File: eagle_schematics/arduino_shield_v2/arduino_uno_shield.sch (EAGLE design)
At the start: 20 parts

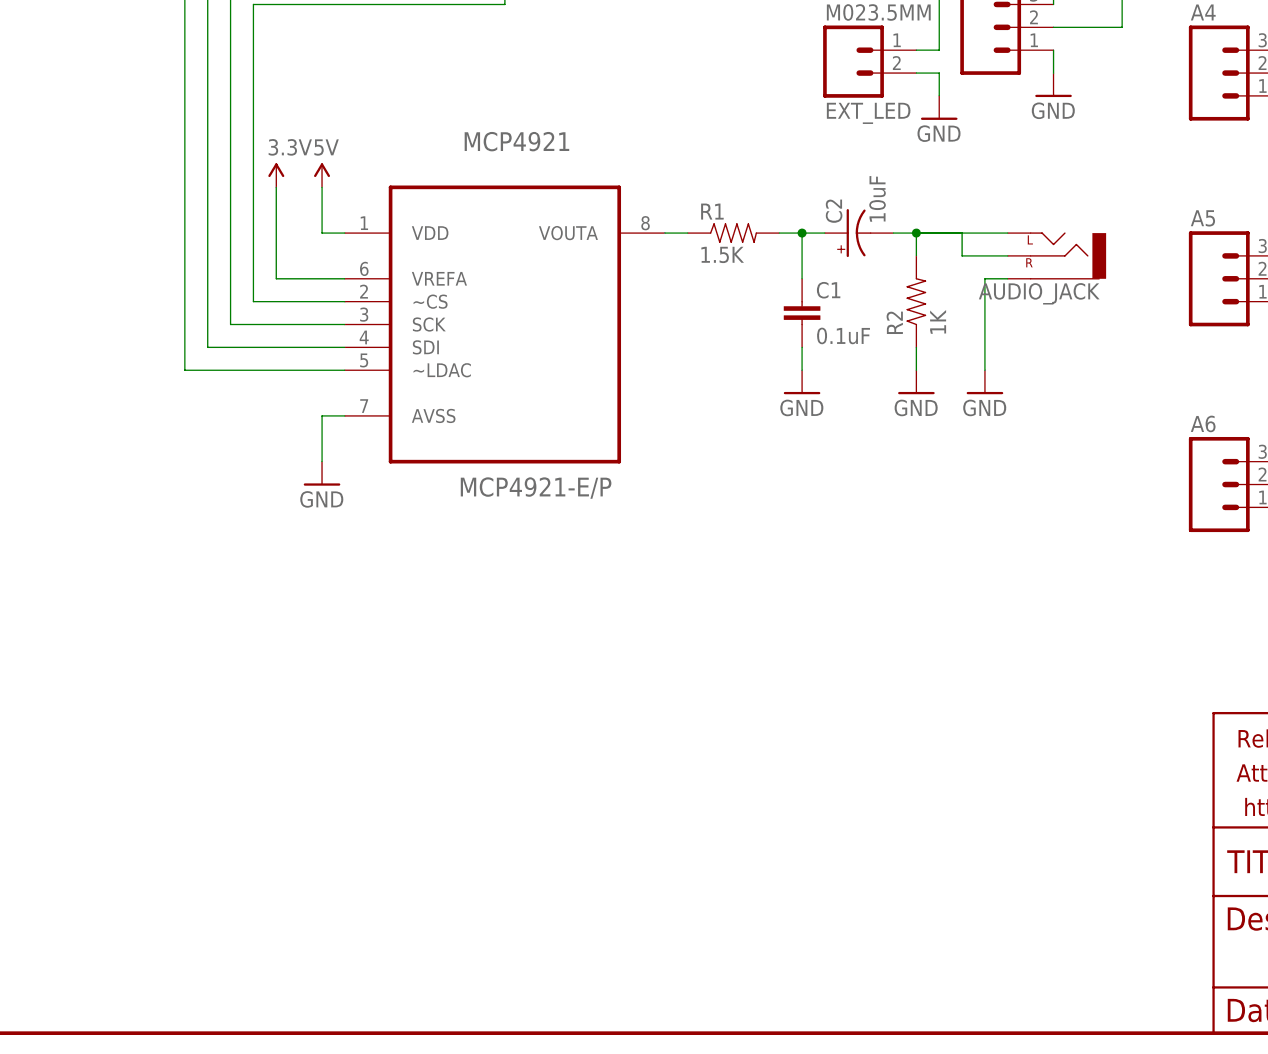
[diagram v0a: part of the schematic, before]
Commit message: add amplifier
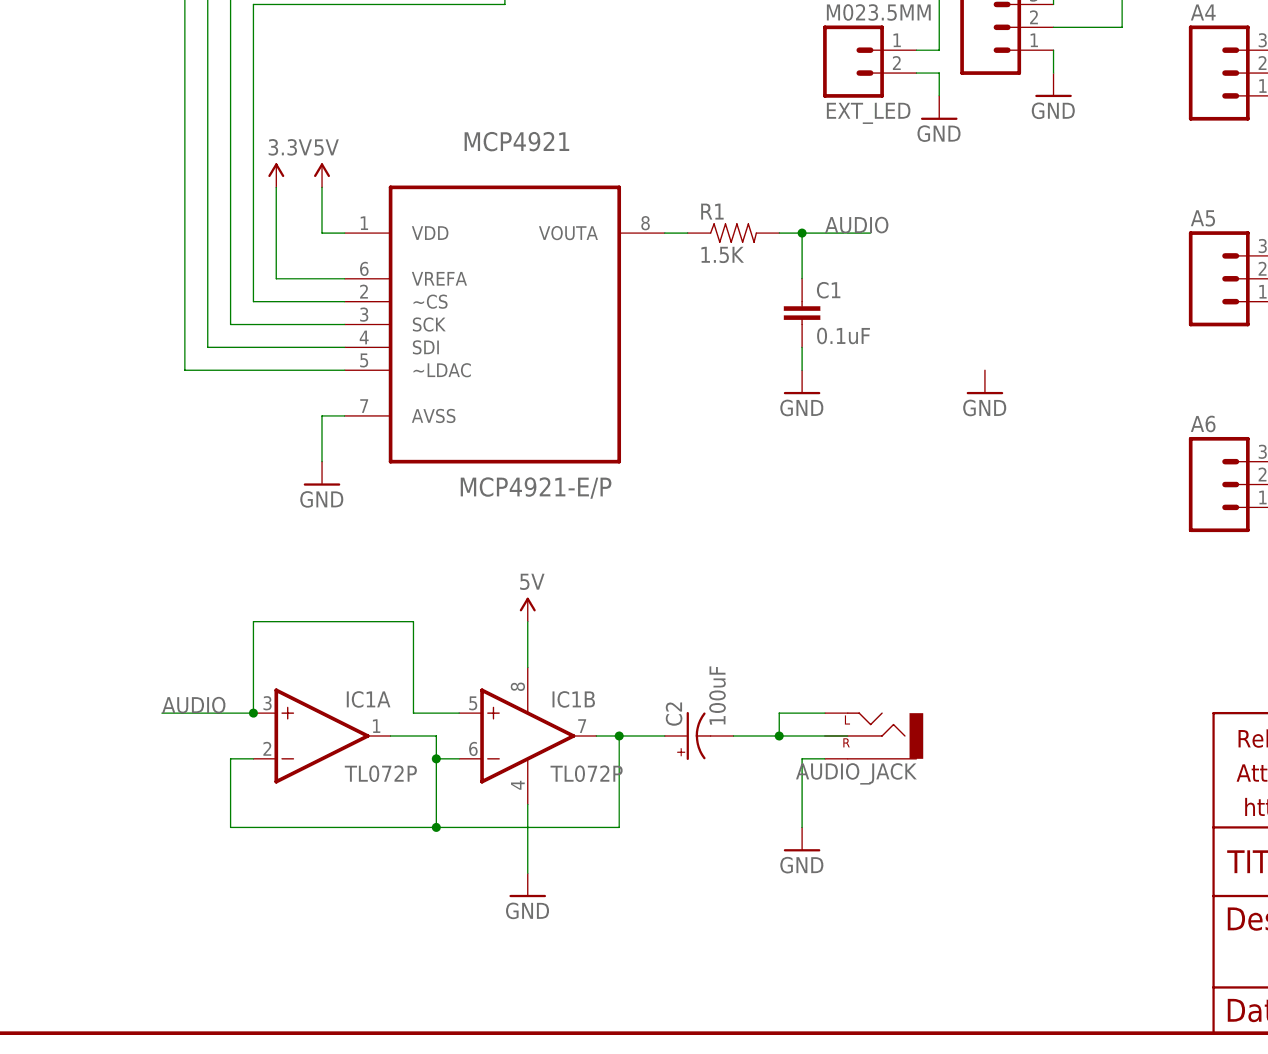
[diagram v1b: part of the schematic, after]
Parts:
- removed R2: 1K, SparkFun-Passives:RESISTORPTH-1/4W
- added IC1: TL072P, linear:TL072P
- C2: value 10uF -> 100uF; device SparkFun-Passives:CAP_POLPTH2 -> SparkFun-Capacitors:CAP_POLPTH1
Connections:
- removed net N$8: C1.1, C2.+, R1.2
- removed net N$9: AUDIO_JACK.LEFT, AUDIO_JACK.RIGHT, C2.-, R2.2
- new net AUDIO: C1.1, IC1A.+IN, IC1B.+IN, R1.2
- new net N$4: C2.+, IC1A.-IN, IC1A.OUT, IC1B.-IN, IC1B.OUT
- new net N$5: AUDIO_JACK.LEFT, C2.-
- net 5V: now also IC1P.V+
- net GND: now also IC1P.V-; no longer R2.1
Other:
- moved on the sheet: AUDIO_JACK, C2
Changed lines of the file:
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@@
 <?xml version="1.0" encoding="utf-8"?>
 <!DOCTYPE eagle SYSTEM "eagle.dtd">
-<eagle version="7.1.0">
+<eagle version="7.5.0">
 <drawing>
 <settings>
@@
 <layer number="223" name="223bmp" color="24" fill="1" visible="no" active="no"/>
 <layer number="224" name="224bmp" color="25" fill="1" visible="no" active="no"/>
+<layer number="225" name="225bmp" color="7" fill="1" visible="yes" active="yes"/>
+<layer number="226" name="226bmp" color="7" fill="1" visible="yes" active="yes"/>
+<layer number="227" name="227bmp" color="7" fill="1" visible="yes" active="yes"/>
+<layer number="228" name="228bmp" color="7" fill="1" visible="yes" active="yes"/>
+<layer number="229" name="229bmp" color="7" fill="1" visible="yes" active="yes"/>
+<layer number="230" name="230bmp" color="7" fill="1" visible="yes" active="yes"/>
+<layer number="231" name="231bmp" color="7" fill="1" visible="yes" active="yes"/>
 <layer number="248" name="Housing" color="7" fill="1" visible="yes" active="yes"/>
 <layer number="249" name="Edge" color="7" fill="1" visible="yes" active="yes"/>
@@
 <layer number="251" name="SMDround" color="12" fill="11" visible="no" active="no"/>
 <layer number="254" name="cooling" color="7" fill="1" visible="yes" active="yes"/>
+<layer number="255" name="routoute" color="7" fill="1" visible="yes" active="yes"/>
 </layers>
 <schematic xreflabel="%F%N/%S.%C%R" xrefpart="/%S.%C%R">
@@
 <part name="MCP4921" library="Microchip_By_element14_Batch_1" deviceset="MCP4921-E/P" device=""/>
 <part name="GND1" library="SparkFun-Aesthetics" deviceset="GND" device=""/>
-<part name="R2" library="SparkFun-Passives" deviceset="RESISTOR" device="PTH-1/4W" value="1K"/>
 <part name="AUDIO_JACK" library="SparkFun-Connectors" deviceset="AUDIO-JACK" device="PTH"/>
 <part name="A1" library="SparkFun-Connectors" deviceset="M03" device="PTH"/>
@@
 <part name="R1" library="SparkFun-Passives" deviceset="RESISTOR" device="PTH-1/4W" value="1.5K"/>
 <part name="C1" library="SparkFun-Passives" deviceset="CAP" device="PTH" value="0.1uF"/>
-<part name="C2" library="SparkFun-Passives" deviceset="CAP_POL" device="PTH2" value="10uF"/>
 <part name="GND6" library="SparkFun-Aesthetics" deviceset="GND" device=""/>
 <part name="GND7" library="SparkFun-Aesthetics" deviceset="GND" device=""/>
@@
 <part name="EXT_LED" library="SparkFun-Connectors" deviceset="M02" device="3.5MM"/>
 <part name="FRAME3" library="SparkFun-Aesthetics" deviceset="FRAME-LETTER" device=""/>
+<part name="IC1" library="linear" deviceset="TL072" device="P"/>
+<part name="SUPPLY15" library="SparkFun-Aesthetics" deviceset="5V" device=""/>
+<part name="C2" library="SparkFun-Capacitors" deviceset="CAP_POL" device="PTH1" value="100uF"/>
+<part name="GND15" library="SparkFun-Aesthetics" deviceset="GND" device=""/>
 </parts>
 <sheets>
@@
 <instance part="MCP4921" gate="A" x="-101.6" y="2.54"/>
 <instance part="GND1" gate="1" x="-68.58" y="-7.62"/>
-<instance part="R2" gate="G$1" x="-55.88" y="2.54" rot="R90"/>
-<instance part="AUDIO_JACK" gate="G$1" x="-40.64" y="7.62" rot="R180"/>
+<instance part="AUDIO_JACK" gate="G$1" x="-60.96" y="-45.72" rot="R180"/>
 <instance part="A1" gate="G$1" x="-48.26" y="55.88" smashed="yes">
 <attribute name="VALUE" x="-50.8" y="48.26" size="1.778" layer="96"/>
@@
 <instance part="R1" gate="G$1" x="-76.2" y="10.16"/>
 <instance part="C1" gate="G$1" x="-68.58" y="0"/>
-<instance part="C2" gate="G$1" x="-63.5" y="10.16" rot="R90"/>
-<instance part="GND6" gate="1" x="-55.88" y="-7.62"/>
+<instance part="GND6" gate="1" x="-99.06" y="-63.5"/>
 <instance part="GND7" gate="1" x="-48.26" y="-7.62"/>
 <instance part="GND8" gate="1" x="-121.92" y="-17.78"/>
@@
 <instance part="FRAME3" gate="G$1" x="-170.18" y="-78.74"/>
 <instance part="FRAME3" gate="G$2" x="-22.86" y="-78.74"/>
+<instance part="IC1" gate="A" x="-121.92" y="-45.72"/>
+<instance part="IC1" gate="B" x="-99.06" y="-45.72"/>
+<instance part="IC1" gate="P" x="-99.06" y="-45.72"/>
+<instance part="SUPPLY15" gate="G$1" x="-99.06" y="-33.02"/>
+<instance part="C2" gate="G$1" x="-81.28" y="-45.72" rot="R90"/>
+<instance part="GND15" gate="1" x="-68.58" y="-58.42"/>
 </instances>
 <busses>
@@
 <pinref part="GND1" gate="1" pin="GND"/>
 <wire x1="-68.58" y1="-2.54" x2="-68.58" y2="-5.08" width="0.1524" layer="91"/>
-</segment>
-<segment>
-<pinref part="R2" gate="G$1" pin="1"/>
-<pinref part="GND6" gate="1" pin="GND"/>
-<wire x1="-55.88" y1="-2.54" x2="-55.88" y2="-5.08" width="0.1524" layer="91"/>
-</segment>
-<segment>
-<pinref part="AUDIO_JACK" gate="G$1" pin="SLEEVE"/>
-<wire x1="-45.72" y1="5.08" x2="-48.26" y2="5.08" width="0.1524" layer="91"/>
-<pinref part="GND7" gate="1" pin="GND"/>
-<wire x1="-48.26" y1="5.08" x2="-48.26" y2="-5.08" width="0.1524" layer="91"/>
 </segment>
 <segment>
@@
 <wire x1="-53.34" y1="27.94" x2="-53.34" y2="25.4" width="0.1524" layer="91"/>
 </segment>
+<segment>
+<pinref part="AUDIO_JACK" gate="G$1" pin="SLEEVE"/>
+<wire x1="-66.04" y1="-48.26" x2="-68.58" y2="-48.26" width="0.1524" layer="91"/>
+<pinref part="GND15" gate="1" pin="GND"/>
+<wire x1="-68.58" y1="-48.26" x2="-68.58" y2="-55.88" width="0.1524" layer="91"/>
+</segment>
+<segment>
+<pinref part="IC1" gate="P" pin="V-"/>
+<pinref part="GND6" gate="1" pin="GND"/>
+<wire x1="-99.06" y1="-53.34" x2="-99.06" y2="-60.96" width="0.1524" layer="91"/>
+</segment>
 </net>
 <net name="5V" class="0">
@@
 <wire x1="-149.86" y1="63.5" x2="-142.24" y2="63.5" width="0.1524" layer="91"/>
 </segment>
+<segment>
+<pinref part="IC1" gate="P" pin="V+"/>
+<pinref part="SUPPLY15" gate="G$1" pin="5V"/>
+<wire x1="-99.06" y1="-38.1" x2="-99.06" y2="-33.02" width="0.1524" layer="91"/>
+</segment>
 </net>
 <net name="3.3V" class="0">
@@
 </segment>
 </net>
-<net name="N$8" class="0">
+<net name="AUDIO" class="0">
 <segment>
 <pinref part="R1" gate="G$1" pin="2"/>
 <wire x1="-71.12" y1="10.16" x2="-68.58" y2="10.16" width="0.1524" layer="91"/>
-<junction x="-68.58" y="10.16"/>
-<pinref part="C2" gate="G$1" pin="+"/>
-<wire x1="-66.04" y1="10.16" x2="-68.58" y2="10.16" width="0.1524" layer="91"/>
 <pinref part="C1" gate="G$1" pin="1"/>
 <wire x1="-68.58" y1="10.16" x2="-68.58" y2="5.08" width="0.1524" layer="91"/>
-</segment>
-</net>
-<net name="N$9" class="0">
-<segment>
-<pinref part="C2" gate="G$1" pin="-"/>
-<wire x1="-58.42" y1="10.16" x2="-55.88" y2="10.16" width="0.1524" layer="91"/>
-<pinref part="R2" gate="G$1" pin="2"/>
-<wire x1="-55.88" y1="10.16" x2="-55.88" y2="7.62" width="0.1524" layer="91"/>
-<junction x="-55.88" y="10.16"/>
-<pinref part="AUDIO_JACK" gate="G$1" pin="LEFT"/>
-<wire x1="-55.88" y1="10.16" x2="-45.72" y2="10.16" width="0.1524" layer="91"/>
-<wire x1="-55.88" y1="10.16" x2="-50.8" y2="10.16" width="0.1524" layer="91"/>
-<wire x1="-50.8" y1="10.16" x2="-50.8" y2="7.62" width="0.1524" layer="91"/>
-<pinref part="AUDIO_JACK" gate="G$1" pin="RIGHT"/>
-<wire x1="-50.8" y1="7.62" x2="-45.72" y2="7.62" width="0.1524" layer="91"/>
+<junction x="-68.58" y="10.16"/>
+<wire x1="-68.58" y1="10.16" x2="-60.96" y2="10.16" width="0.1524" layer="91"/>
+<label x="-66.04" y="10.16" size="1.778" layer="95"/>
+</segment>
+<segment>
+<pinref part="IC1" gate="A" pin="+IN"/>
+<wire x1="-129.54" y1="-43.18" x2="-139.7" y2="-43.18" width="0.1524" layer="91"/>
+<label x="-139.7" y="-43.18" size="1.778" layer="95"/>
+<junction x="-129.54" y="-43.18"/>
+<wire x1="-129.54" y1="-43.18" x2="-129.54" y2="-33.02" width="0.1524" layer="91"/>
+<wire x1="-129.54" y1="-33.02" x2="-111.76" y2="-33.02" width="0.1524" layer="91"/>
+<wire x1="-111.76" y1="-33.02" x2="-111.76" y2="-43.18" width="0.1524" layer="91"/>
+<pinref part="IC1" gate="B" pin="+IN"/>
+<wire x1="-111.76" y1="-43.18" x2="-106.68" y2="-43.18" width="0.1524" layer="91"/>
 </segment>
 </net>
@@
 </segment>
 </net>
+<net name="N$5" class="0">
+<segment>
+<pinref part="C2" gate="G$1" pin="-"/>
+<wire x1="-76.2" y1="-45.72" x2="-71.12" y2="-45.72" width="0.1524" layer="91"/>
+<junction x="-71.12" y="-45.72"/>
+<wire x1="-71.12" y1="-45.72" x2="-63.5" y2="-45.72" width="0.1524" layer="91"/>
+<wire x1="-71.12" y1="-45.72" x2="-71.12" y2="-43.18" width="0.1524" layer="91"/>
+<pinref part="AUDIO_JACK" gate="G$1" pin="LEFT"/>
+<wire x1="-71.12" y1="-43.18" x2="-66.04" y2="-43.18" width="0.1524" layer="91"/>
+</segment>
+</net>
+<net name="N$4" class="0">
+<segment>
+<pinref part="IC1" gate="A" pin="OUT"/>
+<wire x1="-114.3" y1="-45.72" x2="-109.22" y2="-45.72" width="0.1524" layer="91"/>
+<wire x1="-109.22" y1="-45.72" x2="-109.22" y2="-48.26" width="0.1524" layer="91"/>
+<pinref part="IC1" gate="B" pin="-IN"/>
+<wire x1="-109.22" y1="-48.26" x2="-106.68" y2="-48.26" width="0.1524" layer="91"/>
+<junction x="-109.22" y="-48.26"/>
+<wire x1="-109.22" y1="-48.26" x2="-109.22" y2="-55.88" width="0.1524" layer="91"/>
+<wire x1="-109.22" y1="-55.88" x2="-132.08" y2="-55.88" width="0.1524" layer="91"/>
+<wire x1="-132.08" y1="-55.88" x2="-132.08" y2="-48.26" width="0.1524" layer="91"/>
+<pinref part="IC1" gate="A" pin="-IN"/>
+<wire x1="-132.08" y1="-48.26" x2="-129.54" y2="-48.26" width="0.1524" layer="91"/>
+<junction x="-109.22" y="-55.88"/>
+<wire x1="-109.22" y1="-55.88" x2="-88.9" y2="-55.88" width="0.1524" layer="91"/>
+<pinref part="C2" gate="G$1" pin="+"/>
+<pinref part="IC1" gate="B" pin="OUT"/>
+<wire x1="-91.44" y1="-45.72" x2="-88.9" y2="-45.72" width="0.1524" layer="91"/>
+<junction x="-88.9" y="-45.72"/>
+<wire x1="-88.9" y1="-45.72" x2="-83.82" y2="-45.72" width="0.1524" layer="91"/>
+<wire x1="-88.9" y1="-55.88" x2="-88.9" y2="-45.72" width="0.1524" layer="91"/>
+</segment>
+</net>

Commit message: working on new board layout with trimpots
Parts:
- removed A2, A3, A4, A5, A6, A7, A8: (no value), SparkFun-Connectors:M03PTH
- added POT1, POT2, POT3, VOLUME: TSR-3386, SparkFun-Electromechanical:TRIMPOT-PTH-KNOB
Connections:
- removed net N$1: A5.2, MCP3208.CH4
- removed net N$14: A3.2, MCP3208.CH2
- removed net N$15: A4.2, MCP3208.CH3
- removed net N$16: A6.2, MCP3208.CH5
- removed net N$17: A7.2, MCP3208.CH6
- removed net N$18: A8.2, MCP3208.CH7
- removed net N$2: A2.2, MCP3208.CH1
- new net AUDIO2: IC1A.+IN, IC1B.+IN, VOLUME.WIPER
- new net POT1_INPUT: MCP3208.CH1, POT1.WIPER
- new net POT2_INPUT: MCP3208.CH2, POT2.WIPER
- new net POT3_INPUT: MCP3208.CH3, POT3.WIPER
- net 3.3V: now also POT1.CCW, POT2.CCW, POT3.CCW; no longer A2.3, A3.3, A4.3, A5.3, A6.3, A7.3, A8.3
- net AUDIO: now also VOLUME.CCW; no longer IC1A.+IN, IC1B.+IN
- net GND: now also MCP3208.CH4, MCP3208.CH5, MCP3208.CH6, MCP3208.CH7, POT1.CW, POT2.CW, POT3.CW, VOLUME.CW; no longer A2.1, A3.1, A4.1, A5.1, A6.1, A7.1, A8.1
- net N$5: now also AUDIO_JACK.RIGHT

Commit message: change to MCP3204 with 2 trimpot inputs
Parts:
- removed MCP3208: MCP3208-CI/P, Microchip_By_element14_Batch_1:MCP3208-CI/P
- removed POT3: TSR-3386, SparkFun-Electromechanical:TRIMPOT-PTH-KNOB
- added MCP3204: MCP3204-CI/P, Microchip_By_element14_Batch_1:MCP3204-CI/P
- renumbered A1 to MIC
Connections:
- removed net POT3_INPUT: MCP3208.CH3, POT3.WIPER
- net 3.3V: now also MCP3204.VREF; no longer MCP3208.VREF, POT3.CCW
- net 5V: now also MCP3204.VDD; no longer MCP3208.VDD
- net AUD: now also MCP3204.CH0; no longer MCP3208.CH0
- net CS_ADC: now also MCP3204.~CS/SHDN; no longer MCP3208.~CS/SHDN
- net GND: now also MCP3204.AGND, MCP3204.CH3, MCP3204.DGND; no longer MCP3208.AGND, MCP3208.CH4, MCP3208.CH5, MCP3208.CH6, MCP3208.CH7, MCP3208.DGND, POT3.CW
- net POT1_INPUT: now also MCP3204.CH1; no longer MCP3208.CH1
- net POT2_INPUT: now also MCP3204.CH2; no longer MCP3208.CH2
- net SPI_CLK: now also MCP3204.CLK; no longer MCP3208.CLK
- net SPI_MISO: now also MCP3204.DOUT; no longer MCP3208.DOUT
- net SPI_MOSI: now also MCP3204.DIN; no longer MCP3208.DIN

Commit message: refine board layout
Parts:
- removed FRAME3: FRAME-LETTER, SparkFun-Aesthetics:FRAME-LETTER
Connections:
- removed net AUD: MCP3204.CH0, MIC.2
- new net MIC: MCP3204.CH0, MIC.3
- net 3.3V: now also MIC.1; no longer MIC.3
- net GND: now also MIC.2; no longer MIC.1
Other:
- moved on the sheet: MIC
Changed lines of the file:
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@@
 <part name="GND14" library="SparkFun-Aesthetics" deviceset="GND" device=""/>
 <part name="EXT_LED" library="SparkFun-Connectors" deviceset="M02" device="3.5MM"/>
-<part name="FRAME3" library="SparkFun-Aesthetics" deviceset="FRAME-LETTER" device=""/>
 <part name="IC1" library="linear" deviceset="TL072" device="P"/>
 <part name="SUPPLY15" library="SparkFun-Aesthetics" deviceset="5V" device=""/>
@@
 <instance part="GND1" gate="1" x="-68.58" y="-7.62"/>
 <instance part="AUDIO_JACK" gate="G$1" x="-60.96" y="-45.72" rot="R180"/>
-<instance part="MIC" gate="G$1" x="-48.26" y="55.88" smashed="yes">
-<attribute name="VALUE" x="-50.8" y="48.26" size="1.778" layer="96"/>
-<attribute name="NAME" x="-50.8" y="61.722" size="1.778" layer="95"/>
+<instance part="MIC" gate="G$1" x="-40.64" y="55.88" smashed="yes">
+<attribute name="VALUE" x="-43.18" y="48.26" size="1.778" layer="96"/>
+<attribute name="NAME" x="-43.18" y="61.722" size="1.778" layer="95"/>
 </instance>
 <instance part="LED" gate="G$1" x="-63.5" y="50.8"/>
@@
 <instance part="SUPPLY5" gate="G$1" x="-127" y="15.24"/>
 <instance part="SUPPLY6" gate="G$1" x="5.08" y="88.9"/>
-<instance part="SUPPLY7" gate="G$1" x="-40.64" y="60.96"/>
-<instance part="GND4" gate="1" x="-40.64" y="48.26"/>
+<instance part="SUPPLY7" gate="G$1" x="-30.48" y="63.5"/>
+<instance part="GND4" gate="1" x="-25.4" y="43.18"/>
 <instance part="SUPPLY8" gate="G$1" x="-22.86" y="-15.24"/>
 <instance part="GND5" gate="1" x="-22.86" y="-33.02"/>
@@
 <instance part="GND14" gate="1" x="-53.34" y="22.86"/>
 <instance part="EXT_LED" gate="G$1" x="-63.5" y="30.48" rot="MR180"/>
-<instance part="FRAME3" gate="G$1" x="-170.18" y="-78.74"/>
-<instance part="FRAME3" gate="G$2" x="-22.86" y="-78.74"/>
 <instance part="IC1" gate="A" x="-121.92" y="-45.72"/>
 <instance part="IC1" gate="B" x="-99.06" y="-45.72"/>
@@
 </segment>
 <segment>
-<pinref part="MIC" gate="G$1" pin="1"/>
-<pinref part="GND4" gate="1" pin="GND"/>
-<wire x1="-40.64" y1="50.8" x2="-40.64" y2="53.34" width="0.1524" layer="91"/>
-</segment>
-<segment>
 <pinref part="MCP4921" gate="A" pin="AVSS"/>
 <pinref part="GND8" gate="1" pin="GND"/>
@@
 <wire x1="12.7" y1="58.42" x2="15.24" y2="58.42" width="0.1524" layer="91"/>
 </segment>
+<segment>
+<pinref part="MIC" gate="G$1" pin="2"/>
+<wire x1="-33.02" y1="55.88" x2="-25.4" y2="55.88" width="0.1524" layer="91"/>
+<pinref part="GND4" gate="1" pin="GND"/>
+<wire x1="-25.4" y1="55.88" x2="-25.4" y2="45.72" width="0.1524" layer="91"/>
+</segment>
 </net>
 <net name="5V" class="0">
@@
 </segment>
 <segment>
-<pinref part="MIC" gate="G$1" pin="3"/>
-<pinref part="SUPPLY7" gate="G$1" pin="3.3V"/>
-<wire x1="-40.64" y1="58.42" x2="-40.64" y2="60.96" width="0.1524" layer="91"/>
-</segment>
-<segment>
 <pinref part="SUPPLY1" gate="G$1" pin="3.3V"/>
 <wire x1="-157.48" y1="66.04" x2="-157.48" y2="60.96" width="0.1524" layer="91"/>
@@
 <pinref part="POT2" gate="R?" pin="CCW"/>
 <wire x1="5.08" y1="-15.24" x2="5.08" y2="-17.78" width="0.1524" layer="91"/>
+</segment>
+<segment>
+<pinref part="MIC" gate="G$1" pin="1"/>
+<wire x1="-33.02" y1="53.34" x2="-30.48" y2="53.34" width="0.1524" layer="91"/>
+<pinref part="SUPPLY7" gate="G$1" pin="3.3V"/>
+<wire x1="-30.48" y1="53.34" x2="-30.48" y2="63.5" width="0.1524" layer="91"/>
 </segment>
 </net>
@@
 <wire x1="-132.08" y1="38.1" x2="-78.74" y2="38.1" width="0.1524" layer="91"/>
 <wire x1="-78.74" y1="38.1" x2="-78.74" y2="55.88" width="0.1524" layer="91"/>
-</segment>
-</net>
-<net name="AUD" class="0">
-<segment>
-<pinref part="MIC" gate="G$1" pin="2"/>
-<wire x1="-40.64" y1="55.88" x2="-35.56" y2="55.88" width="0.1524" layer="91"/>
-<wire x1="-35.56" y1="55.88" x2="-35.56" y2="66.04" width="0.1524" layer="91"/>
-<pinref part="MCP3204" gate="A" pin="CH0"/>
-<wire x1="-35.56" y1="66.04" x2="15.24" y2="66.04" width="0.1524" layer="91"/>
-<label x="-33.02" y="66.04" size="1.778" layer="95"/>
 </segment>
 </net>
@@
 </segment>
 </net>
+<net name="MIC" class="0">
+<segment>
+<pinref part="MIC" gate="G$1" pin="3"/>
+<wire x1="-33.02" y1="58.42" x2="-17.78" y2="58.42" width="0.1524" layer="91"/>
+<wire x1="-17.78" y1="58.42" x2="-17.78" y2="66.04" width="0.1524" layer="91"/>
+<pinref part="MCP3204" gate="A" pin="CH0"/>
+<wire x1="-17.78" y1="66.04" x2="15.24" y2="66.04" width="0.1524" layer="91"/>
+<label x="-7.62" y="66.04" size="1.778" layer="95"/>
+</segment>
+</net>
